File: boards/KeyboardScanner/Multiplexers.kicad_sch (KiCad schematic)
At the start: 16 parts, among them U1 74LS151, U11 74LS151, U2 74LS151, U3 74LS151, U4 74LS151

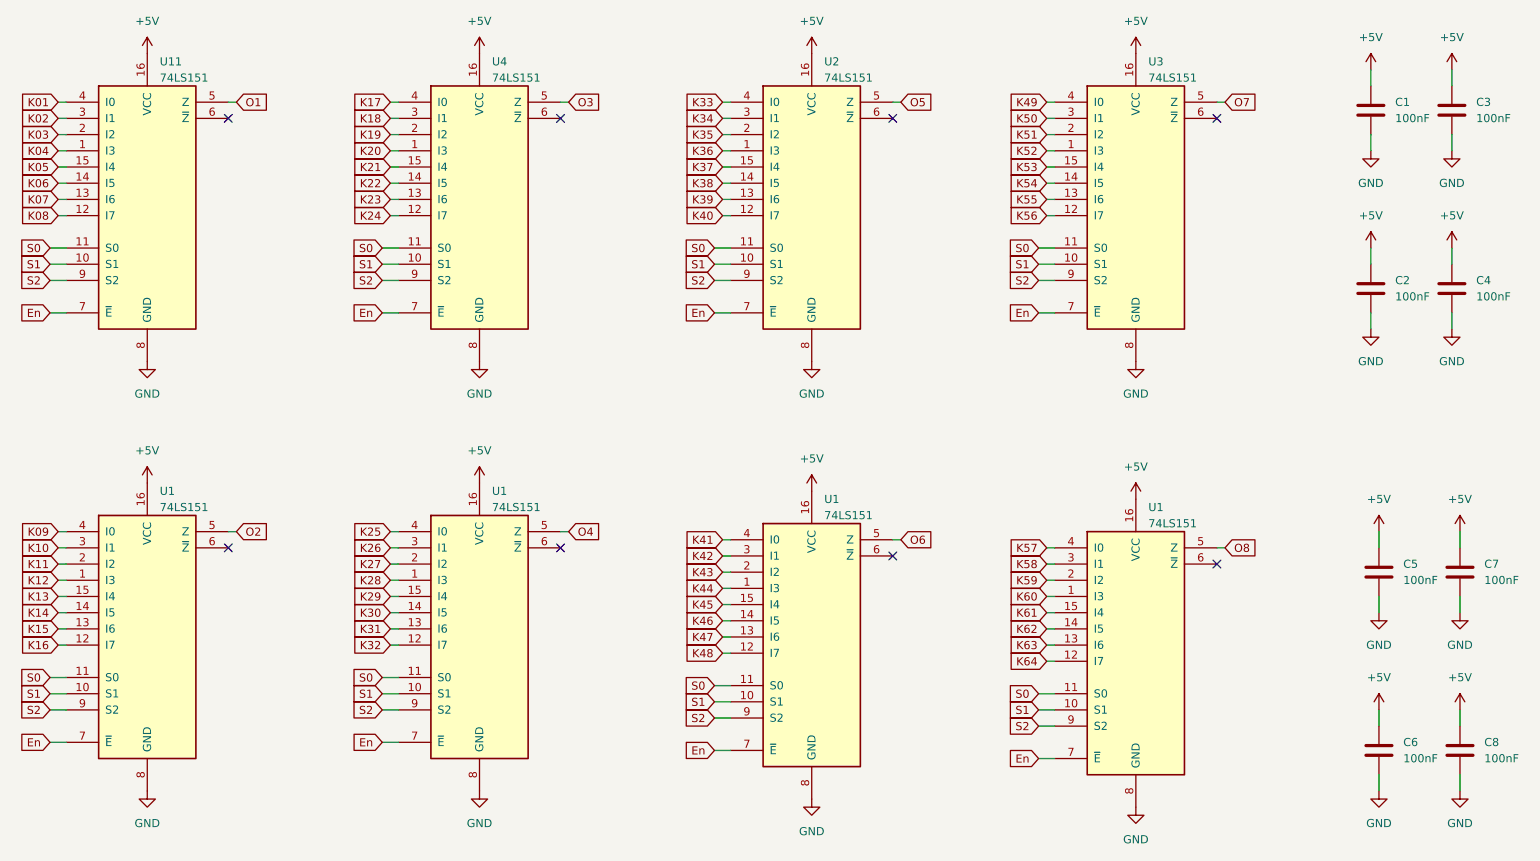
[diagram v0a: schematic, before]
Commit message: PCB layout for keyboard scanner and piston encoder
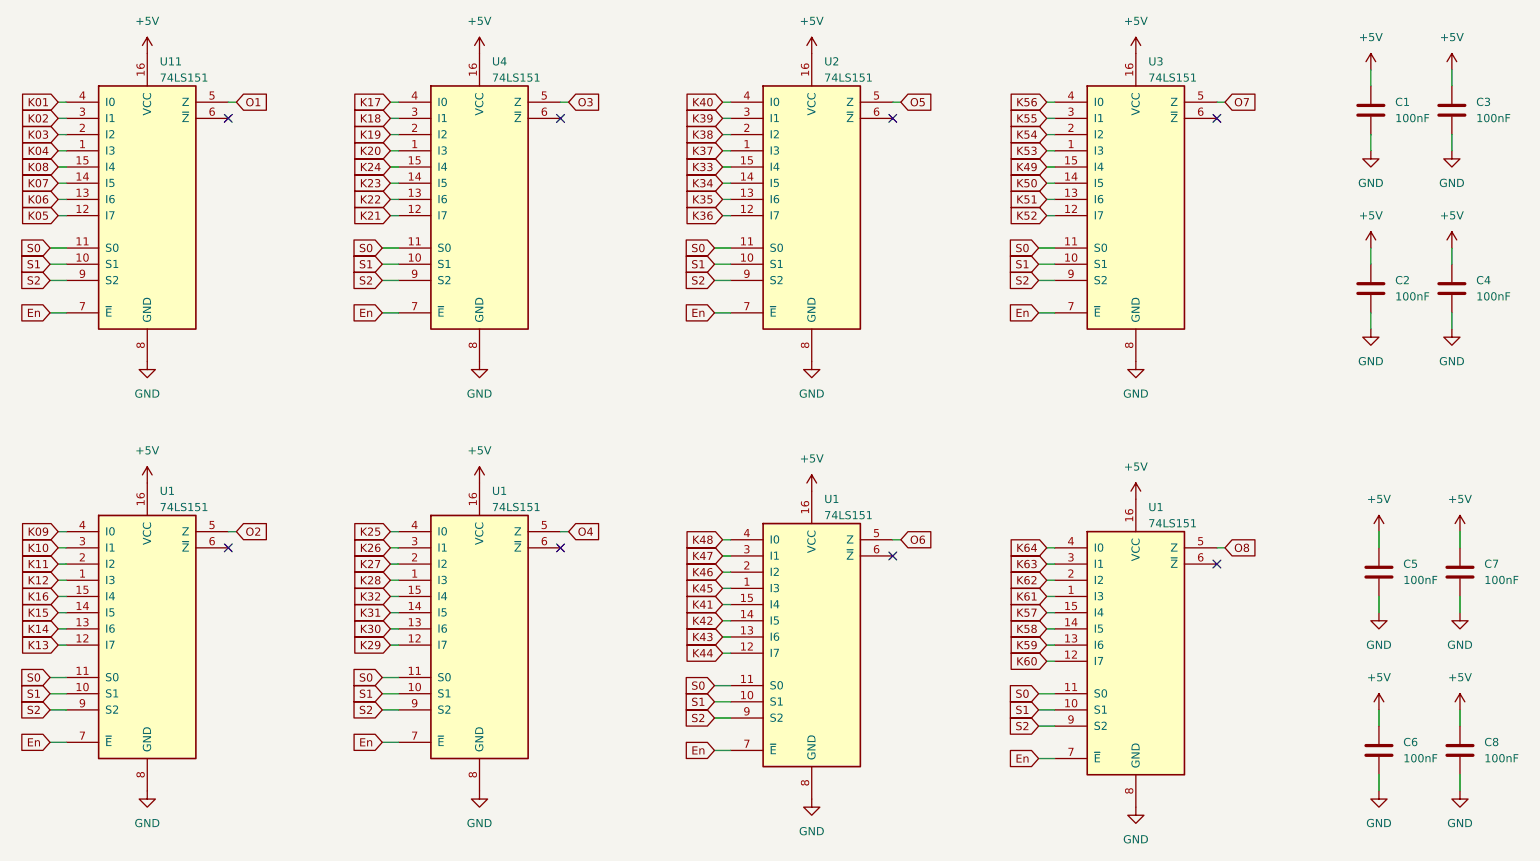
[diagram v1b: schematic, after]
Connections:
- net K05: now also U11.12 (I7); no longer U11.15 (I4)
- net K06: now also U11.13 (I6); no longer U11.14 (I5)
- net K07: now also U11.14 (I5); no longer U11.13 (I6)
- net K08: now also U11.15 (I4); no longer U11.12 (I7)
- net K13: now also U1.12 (I7); no longer U1.15 (I4)
- net K14: now also U1.13 (I6); no longer U1.14 (I5)
- net K15: now also U1.14 (I5); no longer U1.13 (I6)
- net K16: now also U1.15 (I4); no longer U1.12 (I7)
- net K21: now also U4.12 (I7); no longer U4.15 (I4)
- net K22: now also U4.13 (I6); no longer U4.14 (I5)
- net K23: now also U4.14 (I5); no longer U4.13 (I6)
- net K24: now also U4.15 (I4); no longer U4.12 (I7)
- net K29: now also U1.12 (I7); no longer U1.15 (I4)
- net K30: now also U1.13 (I6); no longer U1.14 (I5)
- net K31: now also U1.14 (I5); no longer U1.13 (I6)
- net K32: now also U1.15 (I4); no longer U1.12 (I7)
- net K33: now also U2.15 (I4); no longer U2.4 (I0)
- net K34: now also U2.14 (I5); no longer U2.3 (I1)
- net K35: now also U2.13 (I6); no longer U2.2 (I2)
- net K36: now also U2.12 (I7); no longer U2.1 (I3)
- net K37: now also U2.1 (I3); no longer U2.15 (I4)
- net K38: now also U2.2 (I2); no longer U2.14 (I5)
- net K39: now also U2.3 (I1); no longer U2.13 (I6)
- net K40: now also U2.4 (I0); no longer U2.12 (I7)
- net K41: now also U1.15 (I4); no longer U1.4 (I0)
- net K42: now also U1.14 (I5); no longer U1.3 (I1)
- net K43: now also U1.13 (I6); no longer U1.2 (I2)
- net K44: now also U1.12 (I7); no longer U1.1 (I3)
- net K45: now also U1.1 (I3); no longer U1.15 (I4)
- net K46: now also U1.2 (I2); no longer U1.14 (I5)
- net K47: now also U1.3 (I1); no longer U1.13 (I6)
- net K48: now also U1.4 (I0); no longer U1.12 (I7)
- net K49: now also U3.15 (I4); no longer U3.4 (I0)
- net K50: now also U3.14 (I5); no longer U3.3 (I1)
- net K51: now also U3.13 (I6); no longer U3.2 (I2)
- net K52: now also U3.12 (I7); no longer U3.1 (I3)
- net K53: now also U3.1 (I3); no longer U3.15 (I4)
- net K54: now also U3.2 (I2); no longer U3.14 (I5)
- net K55: now also U3.3 (I1); no longer U3.13 (I6)
- net K56: now also U3.4 (I0); no longer U3.12 (I7)
- net K57: now also U1.15 (I4); no longer U1.4 (I0)
- net K58: now also U1.14 (I5); no longer U1.3 (I1)
- net K59: now also U1.13 (I6); no longer U1.2 (I2)
- net K60: now also U1.12 (I7); no longer U1.1 (I3)
- net K61: now also U1.1 (I3); no longer U1.15 (I4)
- net K62: now also U1.2 (I2); no longer U1.14 (I5)
- net K63: now also U1.3 (I1); no longer U1.13 (I6)
- net K64: now also U1.4 (I0); no longer U1.12 (I7)

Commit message: Updated to KiCAD 8, fixed optocouplers for MIDI and added powersupplies
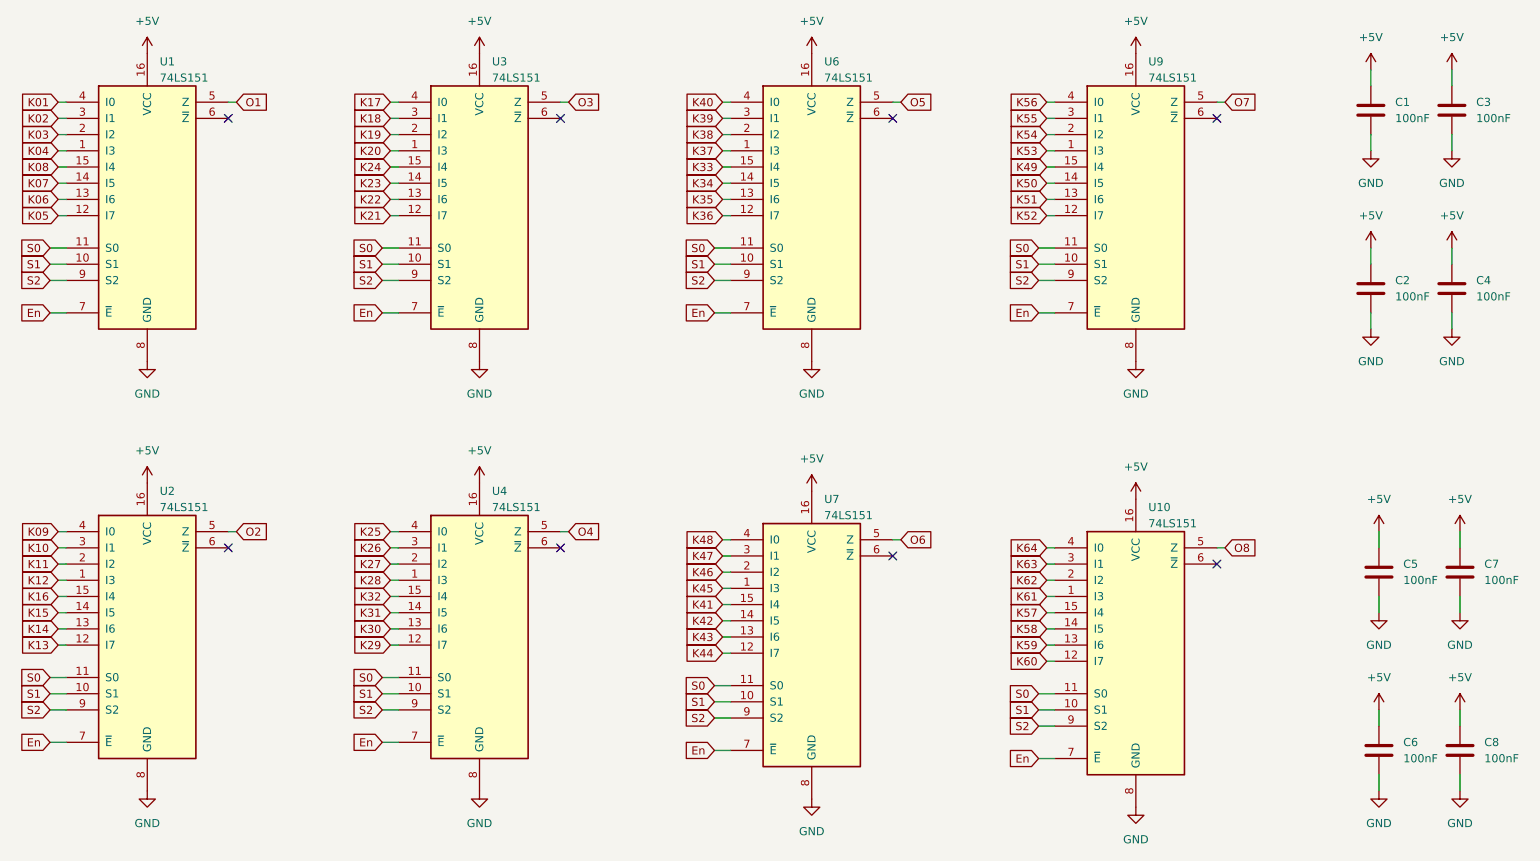
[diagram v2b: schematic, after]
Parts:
- renumbered U11 to U1, U1 to U10, U1 to U2, U4 to U3, U1 to U4, U2 to U6, U1 to U7, U3 to U9

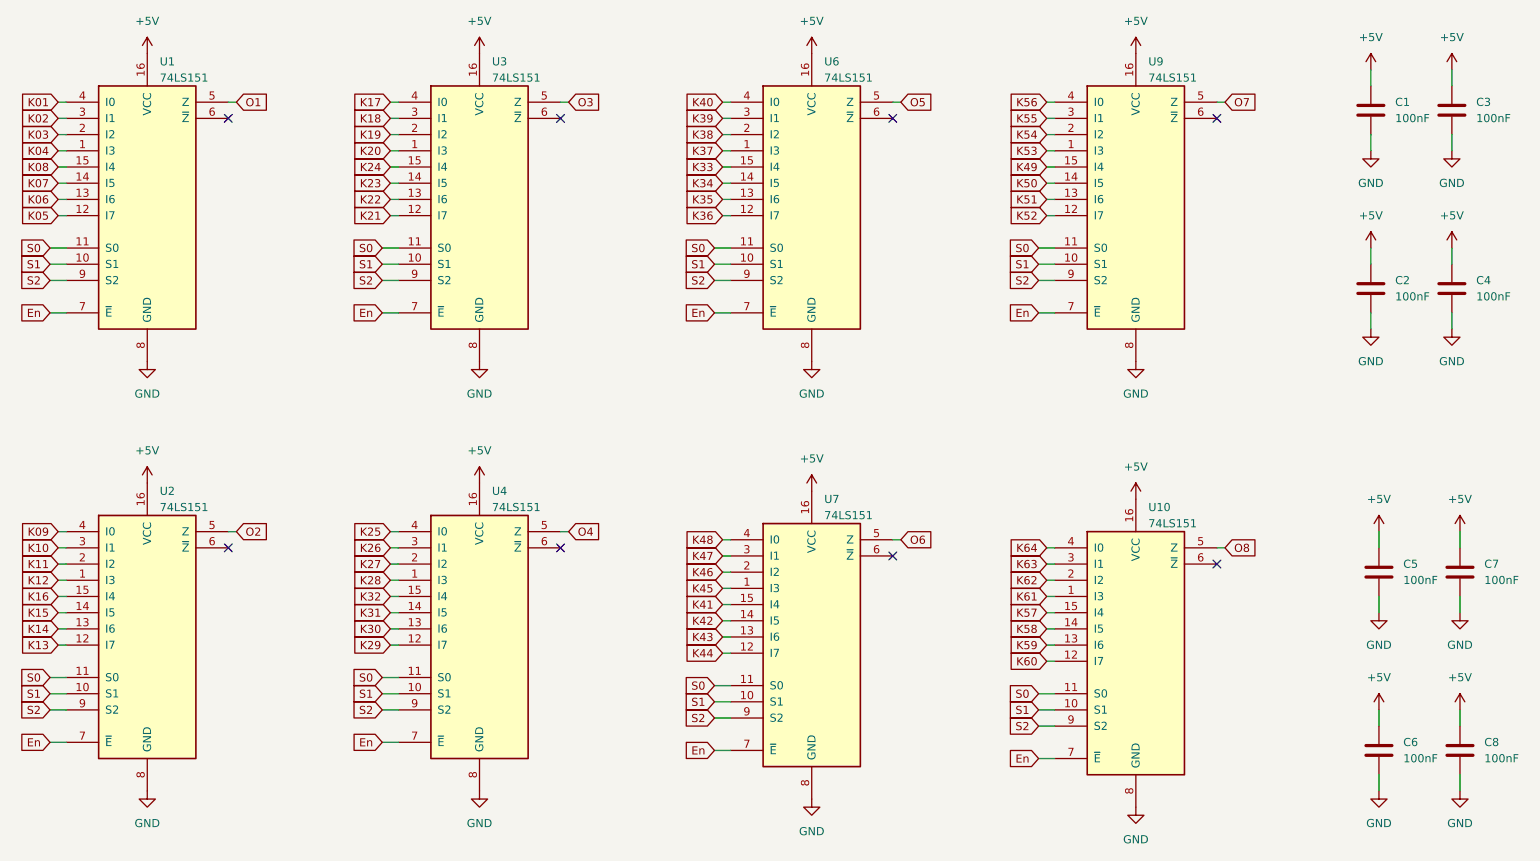
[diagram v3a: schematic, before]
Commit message: Fixed KeyboardScanner schematics to fix open collector enable output
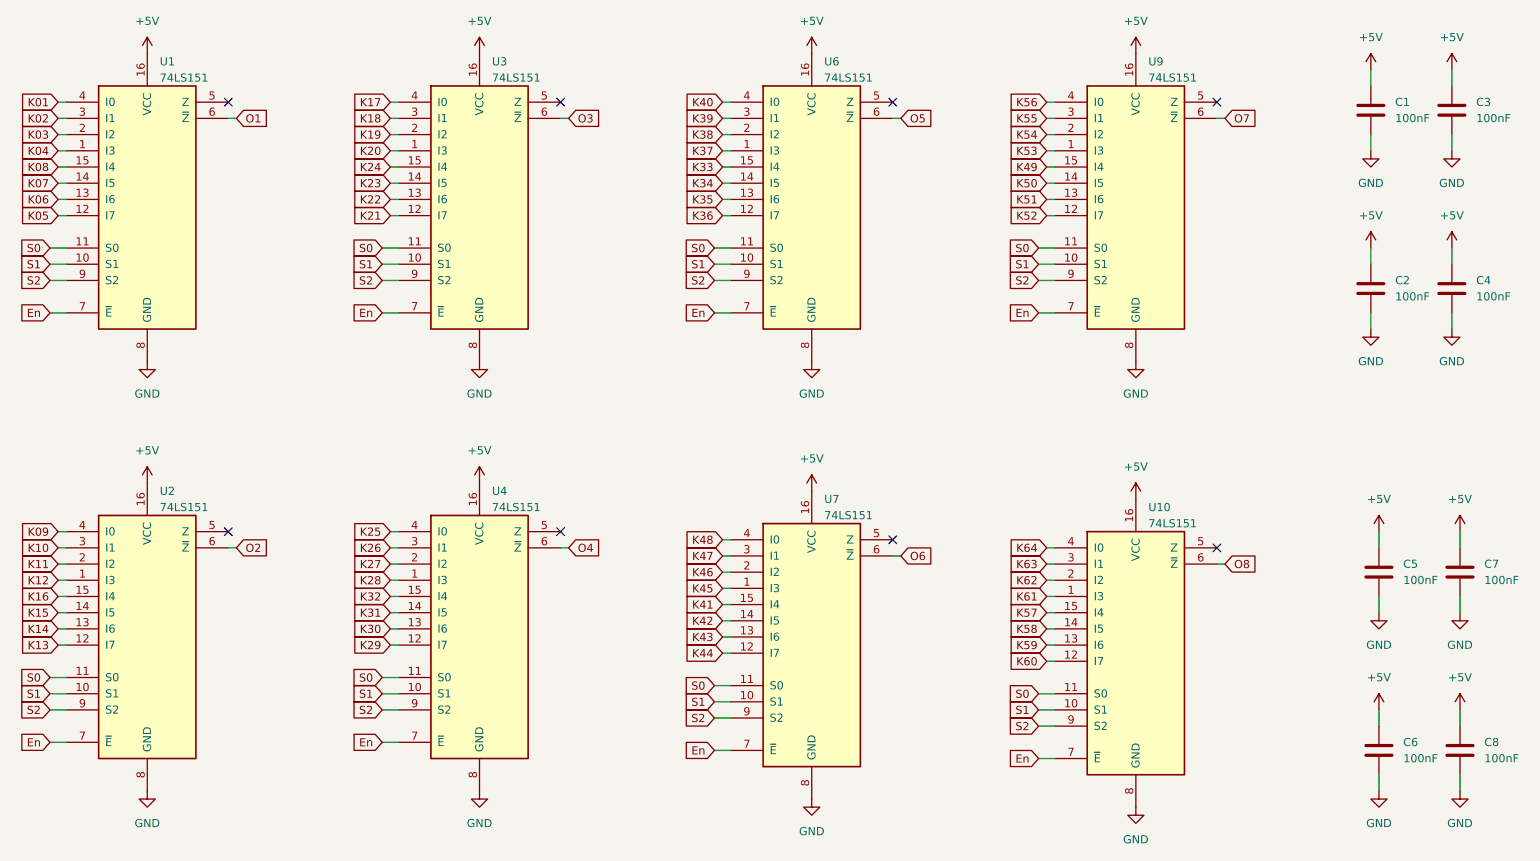
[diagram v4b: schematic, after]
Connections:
- net O1: now also U1.6 (~{Z}); no longer U1.5 (Z)
- net O2: now also U2.6 (~{Z}); no longer U2.5 (Z)
- net O3: now also U3.6 (~{Z}); no longer U3.5 (Z)
- net O4: now also U4.6 (~{Z}); no longer U4.5 (Z)
- net O5: now also U6.6 (~{Z}); no longer U6.5 (Z)
- net O6: now also U7.6 (~{Z}); no longer U7.5 (Z)
- net O7: now also U9.6 (~{Z}); no longer U9.5 (Z)
- net O8: now also U10.6 (~{Z}); no longer U10.5 (Z)
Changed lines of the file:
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@@
 	(paper "A4")
 	(no_connect
-		(at 66.04 41.91)
+		(at 66.04 39.37)
 	)
 	(no_connect
-		(at 170.18 41.91)
+		(at 170.18 39.37)
 	)
 	(no_connect
-		(at 170.18 110.49)
+		(at 170.18 107.95)
 	)
 	(no_connect
-		(at 118.11 41.91)
+		(at 118.11 39.37)
 	)
 	(no_connect
-		(at 220.98 41.91)
+		(at 220.98 39.37)
 	)
 	(no_connect
-		(at 220.98 111.76)
+		(at 220.98 109.22)
 	)
 	(no_connect
-		(at 66.04 109.22)
+		(at 66.04 106.68)
 	)
 	(no_connect
-		(at 118.11 109.22)
+		(at 118.11 106.68)
 	)
 	(wire
@@
 	(wire
 		(pts
-			(xy 170.18 107.95) (xy 171.45 107.95)
+			(xy 170.18 110.49) (xy 171.45 110.49)
+		)
+		(stroke
+			(width 0)
+			(type default)
+		)
+	)
+	(wire
+		(pts
+			(xy 118.11 41.91) (xy 119.38 41.91)
 		)
 		(stroke
@@
 	(wire
 		(pts
-			(xy 66.04 39.37) (xy 67.31 39.37)
+			(xy 66.04 41.91) (xy 67.31 41.91)
 		)
 		(stroke
@@
 	(wire
 		(pts
-			(xy 66.04 106.68) (xy 67.31 106.68)
+			(xy 66.04 109.22) (xy 67.31 109.22)
 		)
 		(stroke
@@
 	(wire
 		(pts
-			(xy 220.98 109.22) (xy 222.25 109.22)
+			(xy 220.98 111.76) (xy 222.25 111.76)
 		)
 		(stroke
@@
 	(wire
 		(pts
-			(xy 118.11 39.37) (xy 119.38 39.37)
-		)
-		(stroke
-			(width 0)
-			(type default)
-		)
-	)
-	(wire
-		(pts
 			(xy 91.44 39.37) (xy 92.71 39.37)
 		)
@@
 	(wire
 		(pts
-			(xy 220.98 39.37) (xy 222.25 39.37)
+			(xy 220.98 41.91) (xy 222.25 41.91)
 		)
 		(stroke
@@
 	(wire
 		(pts
-			(xy 118.11 106.68) (xy 119.38 106.68)
+			(xy 118.11 109.22) (xy 119.38 109.22)
 		)
 		(stroke
@@
 	(wire
 		(pts
-			(xy 170.18 39.37) (xy 171.45 39.37)
+			(xy 170.18 41.91) (xy 171.45 41.91)
 		)
 		(stroke
@@
 	(global_label "O1"
 		(shape input)
-		(at 67.31 39.37 0)
+		(at 67.31 41.91 0)
 		(fields_autoplaced yes)
 		(effects
@@
 		)
 		(property "Intersheetrefs" "${INTERSHEET_REFS}"
-			(at 72.2631 39.2906 0)
+			(at 72.2631 41.8306 0)
 			(effects
 				(font
@@
 	(global_label "O5"
 		(shape input)
-		(at 171.45 39.37 0)
+		(at 171.45 41.91 0)
 		(fields_autoplaced yes)
 		(effects
@@
 		)
 		(property "Intersheetrefs" "${INTERSHEET_REFS}"
-			(at 176.4031 39.2906 0)
+			(at 176.4031 41.8306 0)
 			(effects
 				(font
@@
 	(global_label "O4"
 		(shape input)
-		(at 119.38 106.68 0)
+		(at 119.38 109.22 0)
 		(fields_autoplaced yes)
 		(effects
@@
 		)
 		(property "Intersheetrefs" "${INTERSHEET_REFS}"
-			(at 124.3331 106.6006 0)
+			(at 124.3331 109.1406 0)
 			(effects
 				(font
@@
 	(global_label "O6"
 		(shape input)
-		(at 171.45 107.95 0)
+		(at 171.45 110.49 0)
 		(fields_autoplaced yes)
 		(effects
@@
 		)
 		(property "Intersheetrefs" "${INTERSHEET_REFS}"
-			(at 176.4031 107.8706 0)
+			(at 176.4031 110.4106 0)
 			(effects
 				(font
@@
 	(global_label "O7"
 		(shape input)
-		(at 222.25 39.37 0)
+		(at 222.25 41.91 0)
 		(fields_autoplaced yes)
 		(effects
@@
 		)
 		(property "Intersheetrefs" "${INTERSHEET_REFS}"
-			(at 227.2031 39.2906 0)
+			(at 227.2031 41.8306 0)
 			(effects
 				(font
@@
 	(global_label "O3"
 		(shape input)
-		(at 119.38 39.37 0)
+		(at 119.38 41.91 0)
 		(fields_autoplaced yes)
 		(effects
@@
 		)
 		(property "Intersheetrefs" "${INTERSHEET_REFS}"
-			(at 124.3331 39.2906 0)
+			(at 124.3331 41.8306 0)
 			(effects
 				(font
@@
 	(global_label "O2"
 		(shape input)
-		(at 67.31 106.68 0)
+		(at 67.31 109.22 0)
 		(fields_autoplaced yes)
 		(effects
@@
 		)
 		(property "Intersheetrefs" "${INTERSHEET_REFS}"
-			(at 72.2631 106.6006 0)
+			(at 72.2631 109.1406 0)
 			(effects
 				(font
@@
 	(global_label "O8"
 		(shape input)
-		(at 222.25 109.22 0)
+		(at 222.25 111.76 0)
 		(fields_autoplaced yes)
 		(effects
@@
 		)
 		(property "Intersheetrefs" "${INTERSHEET_REFS}"
-			(at 227.2031 109.1406 0)
-			(effects
-				(font
+			(at 227.2031 111.6806 0)
+			(effects
+				(font
